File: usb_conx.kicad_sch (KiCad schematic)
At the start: 9 parts, among them J56 Conn_01x03, J57 USB_B_Micro, J58 Conn_01x04, U30 TS3USB3000RSE, U31 AP22653AW6-7

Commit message: WIP v0.2.0 changes
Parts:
- removed J56: Conn_01x03, HL_Connector_Pad_2.54mm:Pad_1x03_P2.54_1.7x1.7_Rect-2Oct, symbol Connector_Generic:Conn_01x03
- renumbered J57 to J51, J58 to J52
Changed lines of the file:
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@@
-	(wire
-		(pts
-			(xy 81.28 104.14) (xy 83.82 104.14)
-		)
-		(stroke
-			(width 0)
-			(type default)
-		)
-	)
 	(wire
 		(pts
@@
 	(wire
 		(pts
-			(xy 83.82 106.68) (xy 81.28 106.68)
-		)
-		(stroke
-			(width 0)
-			(type default)
-		)
-	)
-	(wire
-		(pts
 			(xy 182.88 76.2) (xy 182.88 93.98)
 		)
@@
 	(wire
 		(pts
-			(xy 81.28 93.98) (xy 81.28 101.6)
-		)
-		(stroke
-			(width 0)
-			(type default)
-		)
-	)
-	(wire
-		(pts
 			(xy 107.95 87.63) (xy 107.95 85.09)
 		)
@@
 		(pts
 			(xy 180.34 91.44) (xy 170.18 91.44)
-		)
-		(stroke
-			(width 0)
-			(type default)
-		)
-	)
-	(wire
-		(pts
-			(xy 85.09 93.98) (xy 81.28 93.98)
 		)
 		(stroke
@@
 		)
 	)
-	(label "EN"
-		(at 83.82 104.14 0)
-		(effects
-			(font
-				(size 1.27 1.27)
-			)
-			(justify left bottom)
-		)
-	)
 	(label "D+"
 		(at 121.92 74.93 0)
@@
 		)
 	)
-	(label "~{FAULT}"
-		(at 171.45 133.35 0)
-		(effects
-			(font
-				(size 1.27 1.27)
-			)
-			(justify left bottom)
-		)
-	)
 	(label "VBUS"
 		(at 107.95 125.73 180)
@@
 		)
 	)
-	(label "~{FAULT}"
-		(at 83.82 106.68 0)
-		(effects
-			(font
-				(size 1.27 1.27)
-			)
-			(justify left bottom)
-		)
-	)
 	(label "MHL-"
 		(at 170.18 93.98 0)
@@
 		)
 	)
-	(label "EN"
+	(hierarchical_label "EN"
+		(shape input)
+		(at 147.32 92.71 180)
+		(effects
+			(font
+				(size 1.27 1.27)
+			)
+			(justify right)
+		)
+	)
+	(hierarchical_label "~{FAULT}"
+		(shape output)
+		(at 171.45 133.35 0)
+		(effects
+			(font
+				(size 1.27 1.27)
+			)
+			(justify left)
+		)
+	)
+	(hierarchical_label "EN"
+		(shape input)
 		(at 147.32 129.54 180)
 		(effects
@@
 				(size 1.27 1.27)
 			)
-			(justify right bottom)
-		)
-	)
-	(label "EN"
-		(at 147.32 92.71 180)
-		(effects
-			(font
-				(size 1.27 1.27)
-			)
-			(justify right bottom)
+			(justify right)
 		)
 	)
@@
 		(on_board yes)
 		(dnp no)
-		(property "Reference" "#PWR0231"
+		(property "Reference" "#PWR0226"
 			(at 160.02 146.05 0)
 			(effects
@@
 			(project "HALSPA"
 				(path "/7eeba806-440e-4671-bc07-69fe183910a7/e58e5285-b72c-4e4c-88bb-30be4b81421e"
-					(reference "#PWR0231")
+					(reference "#PWR0226")
 					(unit 1)
 				)
@@
 		(dnp no)
 		(fields_autoplaced yes)
-		(property "Reference" "J58"
+		(property "Reference" "J52"
 			(at 190.5 71.1199 0)
 			(effects
@@
 			(project ""
 				(path "/7eeba806-440e-4671-bc07-69fe183910a7/e58e5285-b72c-4e4c-88bb-30be4b81421e"
-					(reference "J58")
+					(reference "J52")
 					(unit 1)
 				)
@@
 		(on_board yes)
 		(dnp no)
-		(property "Reference" "#PWR0226"
+		(property "Reference" "#PWR0221"
 			(at 142.24 146.05 0)
 			(effects
@@
 			(project "HALSPA"
 				(path "/7eeba806-440e-4671-bc07-69fe183910a7/e58e5285-b72c-4e4c-88bb-30be4b81421e"
-					(reference "#PWR0226")
+					(reference "#PWR0221")
 					(unit 1)
 				)
@@
 		(on_board yes)
 		(dnp no)
-		(property "Reference" "#PWR0224"
+		(property "Reference" "#PWR0219"
 			(at 110.49 97.79 0)
 			(effects
@@
 			(project "HALSPA"
 				(path "/7eeba806-440e-4671-bc07-69fe183910a7/e58e5285-b72c-4e4c-88bb-30be4b81421e"
-					(reference "#PWR0224")
+					(reference "#PWR0219")
 					(unit 1)
 				)
@@
 		(dnp no)
 		(fields_autoplaced yes)
-		(property "Reference" "#PWR0230"
+		(property "Reference" "#PWR0225"
 			(at 160.02 106.68 0)
 			(effects
@@
 			(project "HALSPA"
 				(path "/7eeba806-440e-4671-bc07-69fe183910a7/e58e5285-b72c-4e4c-88bb-30be4b81421e"
-					(reference "#PWR0230")
+					(reference "#PWR0225")
 					(unit 1)
 				)
@@
 		(on_board yes)
 		(dnp no)
-		(property "Reference" "#PWR0225"
+		(property "Reference" "#PWR0220"
 			(at 113.03 140.97 0)
 			(effects
@@
 			(project "HALSPA"
 				(path "/7eeba806-440e-4671-bc07-69fe183910a7/e58e5285-b72c-4e4c-88bb-30be4b81421e"
-					(reference "#PWR0225")
-					(unit 1)
-				)
-			)
-		)
-	)
-	(symbol
-		(lib_id "power:GND")
-		(at 85.09 93.98 0)
-		(unit 1)
-		(exclude_from_sim no)
-		(in_bom yes)
-		(on_board yes)
-		(dnp no)
-		(property "Reference" "#PWR0223"
-			(at 85.09 100.33 0)
-			(effects
-				(font
-					(size 1.27 1.27)
-				)
-				(hide yes)
-			)
-		)
-		(property "Value" "GND"
-			(at 85.217 98.3742 0)
-			(effects
-				(font
-					(size 1.27 1.27)
-				)
-			)
-		)
-		(property "Footprint" ""
-			(at 85.09 93.98 0)
-			(effects
-				(font
-					(size 1.27 1.27)
-				)
-				(hide yes)
-			)
-		)
-		(property "Datasheet" ""
-			(at 85.09 93.98 0)
-			(effects
-				(font
-					(size 1.27 1.27)
-				)
-				(hide yes)
-			)
-		)
-		(property "Description" "Power symbol creates a global label with name \"GND\" , ground"
-			(at 85.09 93.98 0)
-			(effects
-				(font
-					(size 1.27 1.27)
-				)
-				(hide yes)
-			)
-		)
-		(pin "1"
-		)
-		(instances
-			(project "HALSPA"
-				(path "/7eeba806-440e-4671-bc07-69fe183910a7/e58e5285-b72c-4e4c-88bb-30be4b81421e"
-					(reference "#PWR0223")
+					(reference "#PWR0220")
 					(unit 1)
 				)
@@
 	)
 	(symbol
-		(lib_id "Connector_Generic:Conn_01x03")
-		(at 76.2 104.14 0)
-		(mirror y)
-		(unit 1)
-		(exclude_from_sim no)
-		(in_bom yes)
-		(on_board yes)
-		(dnp no)
-		(fields_autoplaced yes)
-		(property "Reference" "J56"
-			(at 76.2 95.25 0)
-			(effects
-				(font
-					(size 1.27 1.27)
-				)
-			)
-		)
-		(property "Value" "Conn_01x03"
-			(at 76.2 97.79 0)
-			(effects
-				(font
-					(size 1.27 1.27)
-				)
-			)
-		)
-		(property "Footprint" "HL_Connector_Pad_2.54mm:Pad_1x03_P2.54_1.7x1.7_Rect-2Oct"
-			(at 76.2 104.14 0)
-			(effects
-				(font
-					(size 1.27 1.27)
-				)
-				(hide yes)
-			)
-		)
-		(property "Datasheet" "~"
-			(at 76.2 104.14 0)
-			(effects
-				(font
-					(size 1.27 1.27)
-				)
-				(hide yes)
-			)
-		)
-		(property "Description" "Generic connector, single row, 01x03, script generated (kicad-library-utils/schlib/autogen/connector/)"
-			(at 76.2 104.14 0)
-			(effects
-				(font
-					(size 1.27 1.27)
-				)
-				(hide yes)
-			)
-		)
-		(property "THT_LCSC" ""
-			(at 76.2 104.14 0)
-			(effects
-				(font
-					(size 1.27 1.27)
-				)
-			)
-		)
-		(pin "2"
-		)
-		(pin "3"
-		)
-		(pin "1"
-		)
-		(instances
-			(project ""
-				(path "/7eeba806-440e-4671-bc07-69fe183910a7/e58e5285-b72c-4e4c-88bb-30be4b81421e"
-					(reference "J56")
-					(unit 1)
-				)
-			)
-		)
-	)
-	(symbol
 		(lib_id "HL_Connector:USB_B_Micro")
 		(at 110.49 74.93 0)
@@
 		(on_board yes)
 		(dnp no)
-		(property "Reference" "J57"
+		(property "Reference" "J51"
 			(at 111.9378 63.0682 0)
 			(effects
@@
 			(project "HALSPA"
 				(path "/7eeba806-440e-4671-bc07-69fe183910a7/e58e5285-b72c-4e4c-88bb-30be4b81421e"
-					(reference "J57")
+					(reference "J51")
 					(unit 1)
 				)
@@
 		(dnp no)
 		(fields_autoplaced yes)
-		(property "Reference" "#PWR0228"
+		(property "Reference" "#PWR0223"
 			(at 149.86 101.6 0)
 			(effects
@@
 			(project ""
 				(path "/7eeba806-440e-4671-bc07-69fe183910a7/e58e5285-b72c-4e4c-88bb-30be4b81421e"
-					(reference "#PWR0228")
+					(reference "#PWR0223")
 					(unit 1)
 				)
@@
 		(dnp no)
 		(fields_autoplaced yes)
-		(property "Reference" "#PWR0229"
+		(property "Reference" "#PWR0224"
 			(at 160.02 81.28 0)
 			(effects
@@
 			(project ""
 				(path "/7eeba806-440e-4671-bc07-69fe183910a7/e58e5285-b72c-4e4c-88bb-30be4b81421e"
-					(reference "#PWR0229")
+					(reference "#PWR0224")
 					(unit 1)
 				)
@@
 		(on_board yes)
 		(dnp no)
-		(property "Reference" "#PWR0233"
+		(property "Reference" "#PWR0228"
 			(at 185.42 146.05 0)
 			(effects
@@
 			(project "HALSPA"
 				(path "/7eeba806-440e-4671-bc07-69fe183910a7/e58e5285-b72c-4e4c-88bb-30be4b81421e"
-					(reference "#PWR0233")
+					(reference "#PWR0228")
 					(unit 1)
 				)
@@
 		(dnp no)
 		(fields_autoplaced yes)
-		(property "Reference" "#PWR0227"
+		(property "Reference" "#PWR0222"
 			(at 146.05 85.09 0)
 			(effects
@@
 			(project "HALSPA"
 				(path "/7eeba806-440e-4671-bc07-69fe183910a7/e58e5285-b72c-4e4c-88bb-30be4b81421e"
-					(reference "#PWR0227")
+					(reference "#PWR0222")
 					(unit 1)
 				)
@@
 		(on_board yes)
 		(dnp no)
-		(property "Reference" "#PWR0232"
+		(property "Reference" "#PWR0227"
 			(at 177.8 71.12 0)
 			(effects
@@
 			(project "HALSPA"
 				(path "/7eeba806-440e-4671-bc07-69fe183910a7/e58e5285-b72c-4e4c-88bb-30be4b81421e"
-					(reference "#PWR0232")
+					(reference "#PWR0227")
 					(unit 1)
 				)

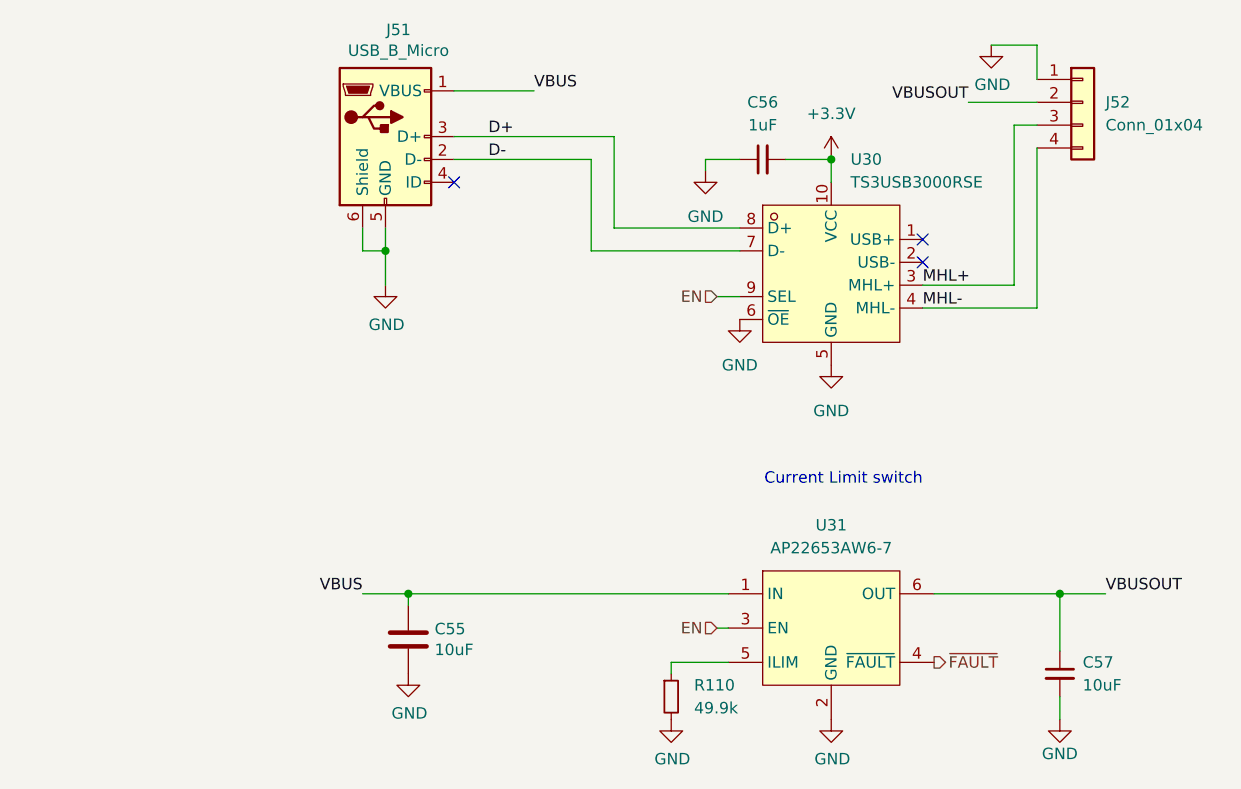
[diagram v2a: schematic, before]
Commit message: Assign part numbers and finish other 0.2.0 changes
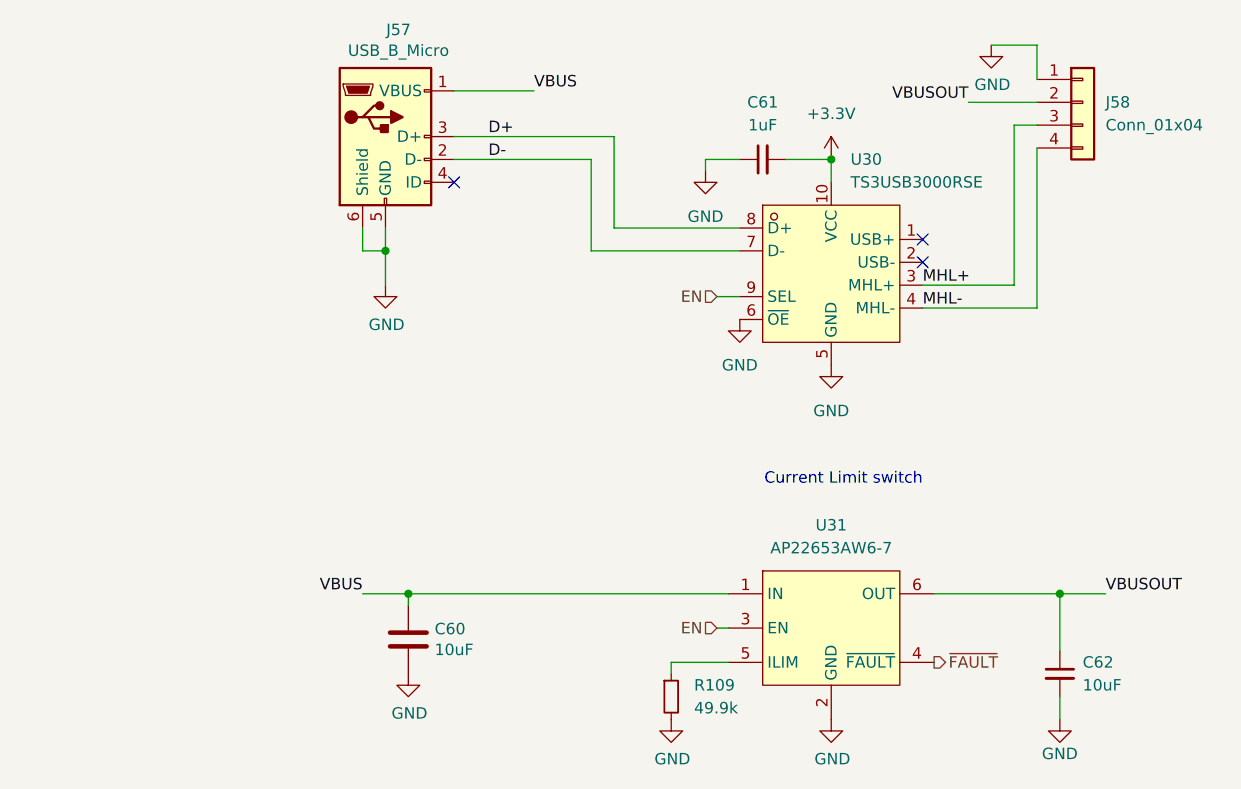
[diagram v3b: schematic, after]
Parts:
- J58: renamed from J52; LCSC (none) -> C2691448
- renumbered C55 to C60, C56 to C61, C57 to C62, J51 to J57, R110 to R109
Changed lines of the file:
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@@
 		(on_board yes)
 		(dnp no)
-		(property "Reference" "C55"
+		(property "Reference" "C60"
 			(at 115.951 129.6416 0)
 			(effects
@@
 			(project "HALSPA"
 				(path "/7eeba806-440e-4671-bc07-69fe183910a7/e58e5285-b72c-4e4c-88bb-30be4b81421e"
-					(reference "C55")
+					(reference "C60")
 					(unit 1)
 				)
@@
 		(on_board yes)
 		(dnp no)
-		(property "Reference" "#PWR0226"
+		(property "Reference" "#PWR0233"
 			(at 160.02 146.05 0)
 			(effects
@@
 			(project "HALSPA"
 				(path "/7eeba806-440e-4671-bc07-69fe183910a7/e58e5285-b72c-4e4c-88bb-30be4b81421e"
-					(reference "#PWR0226")
+					(reference "#PWR0233")
 					(unit 1)
 				)
@@
 		(dnp no)
 		(fields_autoplaced yes)
-		(property "Reference" "J52"
+		(property "Reference" "J58"
 			(at 190.5 71.1199 0)
 			(effects
@@
 			)
 		)
+		(property "LCSC" "C2691448"
+			(at 187.96 71.12 0)
+			(effects
+				(font
+					(size 1.27 1.27)
+				)
+				(hide yes)
+			)
+		)
 		(pin "3"
 		)
@@
 			(project ""
 				(path "/7eeba806-440e-4671-bc07-69fe183910a7/e58e5285-b72c-4e4c-88bb-30be4b81421e"
-					(reference "J52")
+					(reference "J58")
 					(unit 1)
 				)
@@
 		(on_board yes)
 		(dnp no)
-		(property "Reference" "#PWR0221"
+		(property "Reference" "#PWR0228"
 			(at 142.24 146.05 0)
 			(effects
@@
 			(project "HALSPA"
 				(path "/7eeba806-440e-4671-bc07-69fe183910a7/e58e5285-b72c-4e4c-88bb-30be4b81421e"
-					(reference "#PWR0221")
+					(reference "#PWR0228")
 					(unit 1)
 				)
@@
 		(on_board yes)
 		(dnp no)
-		(property "Reference" "#PWR0219"
+		(property "Reference" "#PWR0226"
 			(at 110.49 97.79 0)
 			(effects
@@
 			(project "HALSPA"
 				(path "/7eeba806-440e-4671-bc07-69fe183910a7/e58e5285-b72c-4e4c-88bb-30be4b81421e"
-					(reference "#PWR0219")
+					(reference "#PWR0226")
 					(unit 1)
 				)
@@
 		(dnp no)
 		(fields_autoplaced yes)
-		(property "Reference" "#PWR0225"
+		(property "Reference" "#PWR0232"
 			(at 160.02 106.68 0)
 			(effects
@@
 			(project "HALSPA"
 				(path "/7eeba806-440e-4671-bc07-69fe183910a7/e58e5285-b72c-4e4c-88bb-30be4b81421e"
-					(reference "#PWR0225")
+					(reference "#PWR0232")
 					(unit 1)
 				)
@@
 		(on_board yes)
 		(dnp no)
-		(property "Reference" "#PWR0220"
+		(property "Reference" "#PWR0227"
 			(at 113.03 140.97 0)
 			(effects
@@
 			(project "HALSPA"
 				(path "/7eeba806-440e-4671-bc07-69fe183910a7/e58e5285-b72c-4e4c-88bb-30be4b81421e"
-					(reference "#PWR0220")
+					(reference "#PWR0227")
 					(unit 1)
 				)
@@
 		(on_board yes)
 		(dnp no)
-		(property "Reference" "C57"
+		(property "Reference" "C62"
 			(at 187.96 133.35 0)
 			(effects
@@
 			(project "HALSPA"
 				(path "/7eeba806-440e-4671-bc07-69fe183910a7/e58e5285-b72c-4e4c-88bb-30be4b81421e"
-					(reference "C57")
+					(reference "C62")
 					(unit 1)
 				)
@@
 		(dnp no)
 		(fields_autoplaced yes)
-		(property "Reference" "C56"
+		(property "Reference" "C61"
 			(at 152.4063 71.12 90)
 			(effects
@@
 			(project "HALSPA"
 				(path "/7eeba806-440e-4671-bc07-69fe183910a7/e58e5285-b72c-4e4c-88bb-30be4b81421e"
-					(reference "C56")
+					(reference "C61")
 					(unit 1)
 				)
@@
 		(on_board yes)
 		(dnp no)
-		(property "Reference" "J51"
+		(property "Reference" "J57"
 			(at 111.9378 63.0682 0)
 			(effects
@@
 			(project "HALSPA"
 				(path "/7eeba806-440e-4671-bc07-69fe183910a7/e58e5285-b72c-4e4c-88bb-30be4b81421e"
-					(reference "J51")
+					(reference "J57")
 					(unit 1)
 				)
@@
 		(dnp no)
 		(fields_autoplaced yes)
-		(property "Reference" "#PWR0223"
+		(property "Reference" "#PWR0230"
 			(at 149.86 101.6 0)
 			(effects
@@
 			(project ""
 				(path "/7eeba806-440e-4671-bc07-69fe183910a7/e58e5285-b72c-4e4c-88bb-30be4b81421e"
-					(reference "#PWR0223")
+					(reference "#PWR0230")
 					(unit 1)
 				)
@@
 		(dnp no)
 		(fields_autoplaced yes)
-		(property "Reference" "#PWR0224"
+		(property "Reference" "#PWR0231"
 			(at 160.02 81.28 0)
 			(effects
@@
 			(project ""
 				(path "/7eeba806-440e-4671-bc07-69fe183910a7/e58e5285-b72c-4e4c-88bb-30be4b81421e"
-					(reference "#PWR0224")
+					(reference "#PWR0231")
 					(unit 1)
 				)
@@
 		(on_board yes)
 		(dnp no)
-		(property "Reference" "#PWR0228"
+		(property "Reference" "#PWR0235"
 			(at 185.42 146.05 0)
 			(effects
@@
 			(project "HALSPA"
 				(path "/7eeba806-440e-4671-bc07-69fe183910a7/e58e5285-b72c-4e4c-88bb-30be4b81421e"
-					(reference "#PWR0228")
+					(reference "#PWR0235")
 					(unit 1)
 				)
@@
 		(dnp no)
 		(fields_autoplaced yes)
-		(property "Reference" "#PWR0222"
+		(property "Reference" "#PWR0229"
 			(at 146.05 85.09 0)
 			(effects
@@
 			(project "HALSPA"
 				(path "/7eeba806-440e-4671-bc07-69fe183910a7/e58e5285-b72c-4e4c-88bb-30be4b81421e"
-					(reference "#PWR0222")
+					(reference "#PWR0229")
 					(unit 1)
 				)
@@
 		(on_board yes)
 		(dnp no)
-		(property "Reference" "#PWR0227"
+		(property "Reference" "#PWR0234"
 			(at 177.8 71.12 0)
 			(effects
@@
 			(project "HALSPA"
 				(path "/7eeba806-440e-4671-bc07-69fe183910a7/e58e5285-b72c-4e4c-88bb-30be4b81421e"
-					(reference "#PWR0227")
+					(reference "#PWR0234")
 					(unit 1)
 				)
@@
 		(dnp no)
 		(fields_autoplaced yes)
-		(property "Reference" "R110"
+		(property "Reference" "R109"
 			(at 144.78 135.8899 0)
 			(effects
@@
 			(project ""
 				(path "/7eeba806-440e-4671-bc07-69fe183910a7/e58e5285-b72c-4e4c-88bb-30be4b81421e"
-					(reference "R110")
-					(unit 1)
-				)
+					(reference "R109")
+					(unit 1)
+				)

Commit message: Update the title blocks
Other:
- company: (none) -> Hat Labs Oy
- title: (none) -> HALSPA - Hat Labs Spaghetti Board
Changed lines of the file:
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@@
 	(generator_version "9.0")
 	(paper "A4")
+	(title_block
+		(title "HALSPA - Hat Labs Spaghetti Board")
+		(date "2025-04-17")
+		(rev "v0.2.0")
+		(company "Hat Labs Oy")
+		(comment 1 "See the accompanying LICENSE.md file for license details.")
+	)
 	(text "Current Limit switch"
 		(exclude_from_sim no)

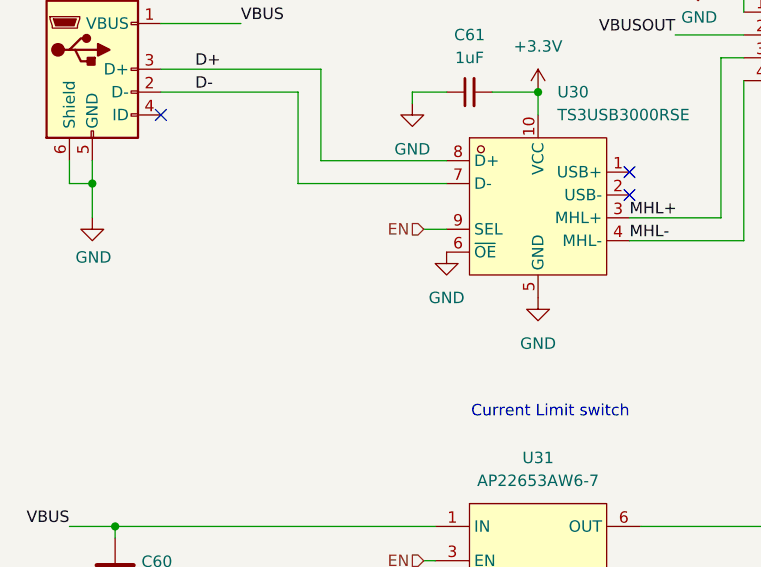
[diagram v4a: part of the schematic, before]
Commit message: Add JLCPCB corrections
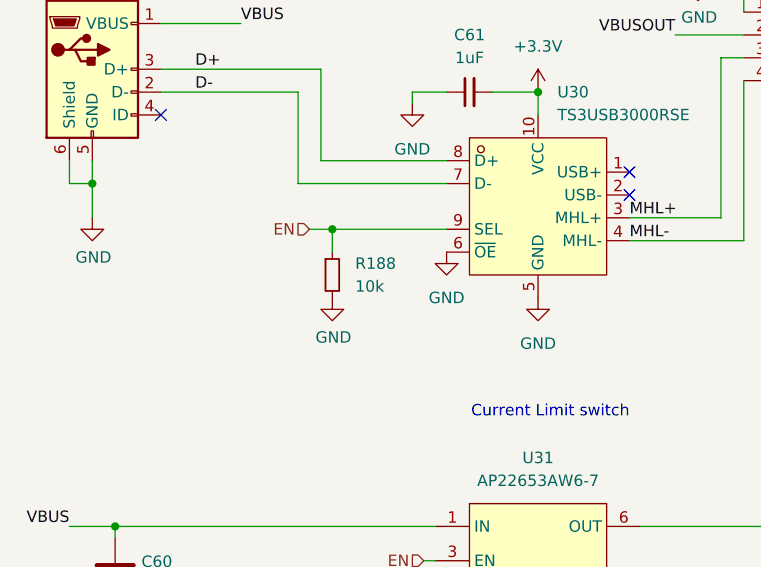
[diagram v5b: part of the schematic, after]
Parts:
- added R188: 10k, Resistor_SMD:R_0603_1608Metric_Pad0.98x0.95mm_HandSolder, symbol Device:R_Small
- J57: JLCPCB_CORRECTION 1.3;0.5;0 -> (none)
- J58: JLCPCB_CORRECTION (none) -> 0;3.81;270
- U31: JLCPCB_CORRECTION 0;0;90 -> 0;0;270
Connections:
- net EN: now also R188.1
- net GND: now also R188.2
